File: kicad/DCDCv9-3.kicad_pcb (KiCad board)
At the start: 4 copper layers, 85.6 x 54 mm, 215 parts, among them J1 Screw_Terminal_01x03, J2 Conn_01x02_Male, J3 Conn_01x02, J4 Conn_01x02_Male, J5 XT60 Male, J6 Conn_01x02_Male, J7 Conn_01x02_Male, J8 Conn_01x02_Male, Q1 PMV20ENR, Q10 IMBG65R050M2HXTMA1, Q11 IMBG65R050M2HXTMA1, Q2 PMV20ENR, Q3 SIHP24N80AE-GE3, Q4 IXYP8N90C3, Q5 PMV20ENR, Q6 PMV20ENR, Q7 PMV20ENR, Q8 BSC027N06LS5ATMA1, Q9 BSC027N06LS5ATMA1, T1 DIY Transformer ETD 39, U1 TBA 1-1212HI, U10 LM2904BIDDFR, U11 UCC21520DW, U12 UCC25600, U13 ZXRE330ASA-7, U14 LM2904BIDDFR, U2 RT9058-90GVL, U3 MP4541_SOP8-EP, U4 TLV61048DBVR, U5 NCP4305DMTTWG, U6 LM2904BIDDFR, U7 TL431, U8 NCP4305DMTTWG, U9 ACPL-217-50AE

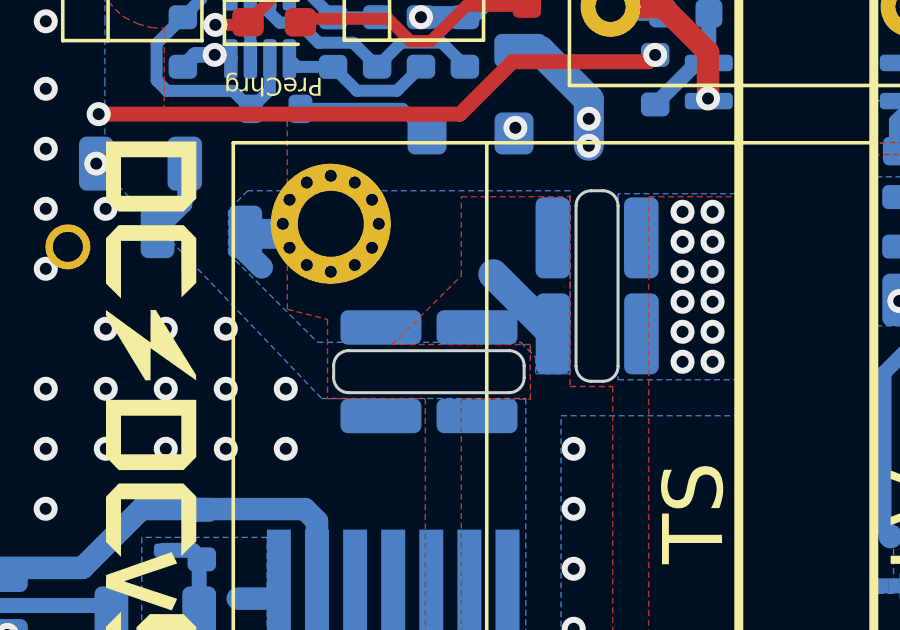
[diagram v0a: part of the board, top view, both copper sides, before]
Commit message: adjusted creepage distance
The closest inner layer to outer layer, which uses a prepreg of 0.21 mm, would result in 0.81 mm creepage distance on edges. Due to unknown IPC 2221 rating for this case, the design was adjusted (below the gate driver and a trace below the resonant capacitors) from 0.3 mm to 0.6 mm to be safe.
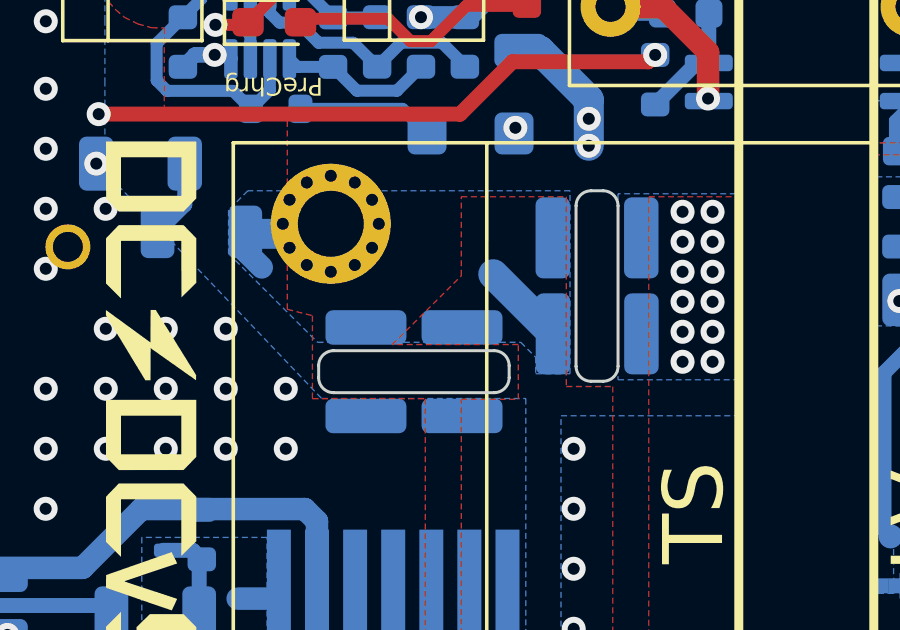
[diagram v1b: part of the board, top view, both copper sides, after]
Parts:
- moved C36 0.50 mm to (136.4, 96.4)
- moved C37 0.50 mm to (133.2, 96.4)
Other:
- outline, holes or cut-outs redrawn
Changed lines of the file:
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@@
 	(footprint "DCDC-Footprints:C_1210_3225Metric"
 		(layer "B.Cu")
-		(at 136.865 96.435 -90)
+		(at 136.365 96.435 -90)
 		(descr "Capacitor SMD 1210 (3225 Metric), square (rectangular) end terminal, IPC_7351 nominal, (Body size source: IPC-SM-782 page 76, https://www.pcb-3d.com/wordpress/wp-content/uploads/ipc-sm-782a_amendment_1_and_2.pdf), generated with kicad-footprint-generator")
 		(tags "capacitor")
@@
 	(footprint "DCDC-Footprints:C_1210_3225Metric"
 		(layer "B.Cu")
-		(at 133.661905 96.43674 -90)
+		(at 133.161905 96.43674 -90)
 		(descr "Capacitor SMD 1210 (3225 Metric), square (rectangular) end terminal, IPC_7351 nominal, (Body size source: IPC-SM-782 page 76, https://www.pcb-3d.com/wordpress/wp-content/uploads/ipc-sm-782a_amendment_1_and_2.pdf), generated with kicad-footprint-generator")
 		(tags "capacitor")
@@
 	)
 	(gr_line
-		(start 132.585 95.735)
-		(end 137.935 95.735)
+		(start 132.085 95.735)
+		(end 137.435 95.735)
 		(stroke
 			(width 0.1)
@@
 	)
 	(gr_arc
-		(start 132.585 97.135)
-		(mid 132.231447 96.988553)
-		(end 132.085 96.635)
+		(start 132.085 97.135)
+		(mid 131.731447 96.988553)
+		(end 131.585 96.635)
 		(stroke
 			(width 0.1)
@@
 	)
 	(gr_arc
-		(start 138.435 96.635)
-		(mid 138.288553 96.988553)
-		(end 137.935 97.135)
+		(start 137.935 96.635)
+		(mid 137.788553 96.988553)
+		(end 137.435 97.135)
 		(stroke
 			(width 0.1)
@@
 	)
 	(gr_arc
-		(start 137.935 95.735)
-		(mid 138.288553 95.881447)
-		(end 138.435 96.235)
+		(start 137.435 95.735)
+		(mid 137.788553 95.881447)
+		(end 137.935 96.235)
 		(stroke
 			(width 0.1)
@@
 	)
 	(gr_arc
-		(start 132.085 96.235)
-		(mid 132.231447 95.881447)
-		(end 132.585 95.735)
+		(start 131.585 96.235)
+		(mid 131.731447 95.881447)
+		(end 132.085 95.735)
 		(stroke
 			(width 0.1)
@@
 	)
 	(gr_line
-		(start 132.085 96.635)
-		(end 132.085 96.235)
+		(start 131.585 96.635)
+		(end 131.585 96.235)
 		(stroke
 			(width 0.1)
@@
 	)
 	(gr_line
-		(start 137.935 97.135)
-		(end 132.585 97.135)
+		(start 137.435 97.135)
+		(end 132.085 97.135)
 		(stroke
 			(width 0.1)
@@
 	)
 	(gr_line
-		(start 138.435 96.235)
-		(end 138.435 96.635)
+		(start 137.935 96.235)
+		(end 137.935 96.635)
 		(stroke
 			(width 0.1)
@@
 	)
 	(segment
-		(start 140.59 89.205)
-		(end 139.3 90.495)
+		(start 139.05 97.371855)
+		(end 137.396855 99.025)
 		(width 1)
 		(layer "In2.Cu")
@@
 	)
 	(segment
-		(start 137.396855 99.028145)
-		(end 137.396855 104.848145)
+		(start 140.59 88.905)
+		(end 140.59 88.955)
 		(width 1)
 		(layer "In2.Cu")
@@
 	(segment
 		(start 137.396855 104.848145)
-		(end 134.79 107.455)
+		(end 137.396855 99.025)
+		(width 1)
+		(layer "In2.Cu")
+		(net 56)
+	)
+	(segment
+		(start 140.59 88.955)
+		(end 139.05 90.495)
 		(width 1)
 		(layer "In2.Cu")
@@
 	)
 	(segment
-		(start 139.3 97.125)
-		(end 137.396855 99.028145)
+		(start 134.79 107.455)
+		(end 126.13 107.455)
 		(width 1)
 		(layer "In2.Cu")
@@
 	)
 	(segment
-		(start 140.59 89.205)
+		(start 140.59 88.905)
 		(end 140.59 88.005)
 		(width 1)
@@
 	)
 	(segment
-		(start 134.79 107.455)
-		(end 126.13 107.455)
+		(start 139.05 90.495)
+		(end 139.05 97.371855)
 		(width 1)
 		(layer "In2.Cu")
@@
 	)
 	(segment
-		(start 139.3 90.495)
-		(end 139.3 97.125)
+		(start 137.396855 104.848145)
+		(end 134.79 107.455)
 		(width 1)
 		(layer "In2.Cu")
@@
 		(hatch edge 0.508)
 		(connect_pads yes
-			(clearance 0.2)
+			(clearance 0.3)
 		)
 		(min_thickness 0.2)
@@
 				(xy 141.39 96.93) (xy 141.39 124.505) (xy 120.79 124.505) (xy 120.79 112.527097) (xy 117.84 112.527097)
 				(xy 117.84 109.055) (xy 127.73 109.055) (xy 127.73 107.105) (xy 136.34 107.105) (xy 136.34 97.355)
-				(xy 138.64 97.355) (xy 138.64 95.53) (xy 134.040127 95.53) (xy 136.34 93.241743) (xy 136.34 90.605)
-				(xy 139.965 90.605) (xy 139.965 96.93)
+				(xy 138.24 97.355) (xy 138.24 95.53) (xy 134.040127 95.53) (xy 136.34 93.241743) (xy 136.34 90.605)
+				(xy 139.84 90.605) (xy 139.84 96.93)
 			)
 		)
@@
 				(xy 124.237796 83.362886) (xy 124.26 83.455) (xy 124.345872 83.71) (xy 124.59 84.11) (xy 124.81986 84.37)
 				(xy 125.108608 84.62) (xy 125.561708 84.843826) (xy 126.021098 84.97) (xy 126.438931 84.98) (xy 126.438931 87.755)
-				(xy 130.54 87.755) (xy 130.54 94.355) (xy 130.537059 94.355) (xy 131.879563 94.695) (xy 131.880027 97.335)
+				(xy 130.54 87.755) (xy 130.54 94.355) (xy 130.537059 94.355) (xy 131.37864 94.568137) (xy 131.379126 97.335)
 				(xy 135.14 97.335) (xy 135.14 105.855) (xy 117.84 105.855) (xy 117.84 101.005) (xy 115.24 101.005)
 				(xy 115.24 101.33) (xy 106.89 101.33) (xy 106.89 95.705) (xy 107.14 95.705) (xy 107.14 83.755) (xy 108.39 82.505)
@@
 		(polygon
 			(pts
-				(xy 124.565 87.805) (xy 130.59 87.805) (xy 130.59 90.98) (xy 130.59 92.805) (xy 131.88 92.805) (xy 131.88 97.335)
+				(xy 124.565 87.805) (xy 130.59 87.805) (xy 130.59 90.98) (xy 130.59 92.805) (xy 131.38 92.805) (xy 131.38 97.335)
 				(xy 137.89 97.335) (xy 137.89 105.005) (xy 134.94 107.955) (xy 127.335531 107.955) (xy 127.335531 106.255)
-				(xy 117.89 106.255) (xy 117.89 101.005) (xy 115.24 101.005) (xy 115.24 108.205) (xy 102.79 108.205)
+				(xy 117.89 106.255) (xy 117.89 101.005) (xy 114.94 101.005) (xy 114.94 108.205) (xy 102.79 108.205)
 				(xy 102.79 101.505) (xy 100.29 101.505) (xy 100.29 95.705) (xy 107.14 95.705) (xy 107.14 83.755)
 				(xy 108.39 82.505) (xy 121.64 82.505) (xy 122.49 81.655) (xy 122.49 79.33) (xy 124.29909 79.33)
@@
 		(polygon
 			(pts
-				(xy 100.29 109.405) (xy 115.24 109.405) (xy 115.24 113.205) (xy 115.765 113.73) (xy 119.99 113.73)
+				(xy 100.29 109.405) (xy 114.94 109.405) (xy 114.94 112.905) (xy 115.765 113.73) (xy 119.99 113.73)
 				(xy 119.99 125.305) (xy 127.99 125.305) (xy 127.99 128.705) (xy 100.29 128.705)
 			)
@@
 		(polygon
 			(pts
-				(xy 124.565 87.805) (xy 130.59 87.805) (xy 130.59 92.805) (xy 131.88 92.805) (xy 131.88 97.335)
+				(xy 124.565 87.805) (xy 130.59 87.805) (xy 130.59 92.805) (xy 131.38 92.805) (xy 131.38 97.335)
 				(xy 135.84 97.335) (xy 135.84 104.33) (xy 134.015 106.155) (xy 117.84 106.155) (xy 117.84 101.005)
 				(xy 115.24 101.005) (xy 115.24 112.655) (xy 106.69 112.655) (xy 106.69 108.605) (xy 102.79 108.605)

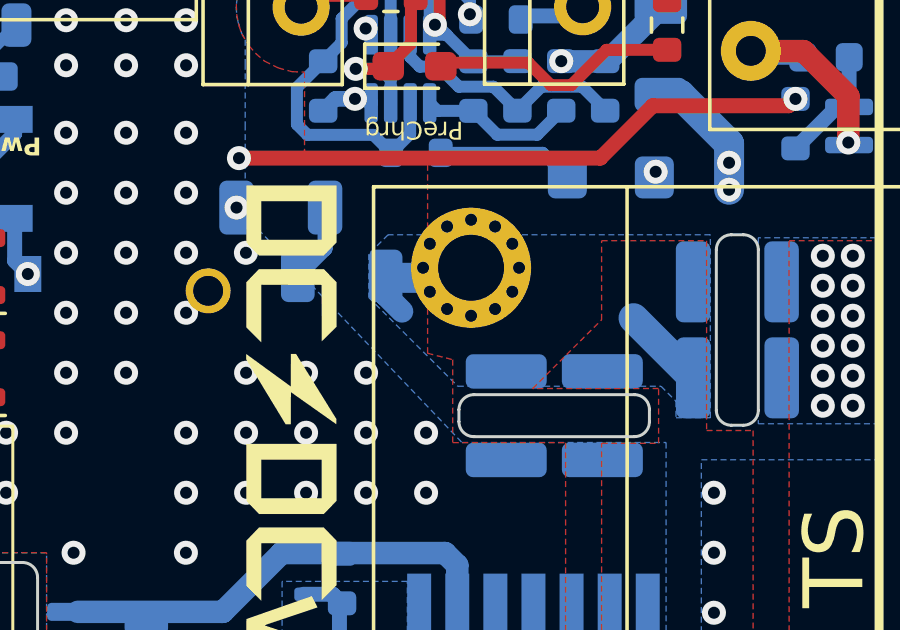
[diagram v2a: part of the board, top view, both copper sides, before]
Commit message: increased clearance a bit more
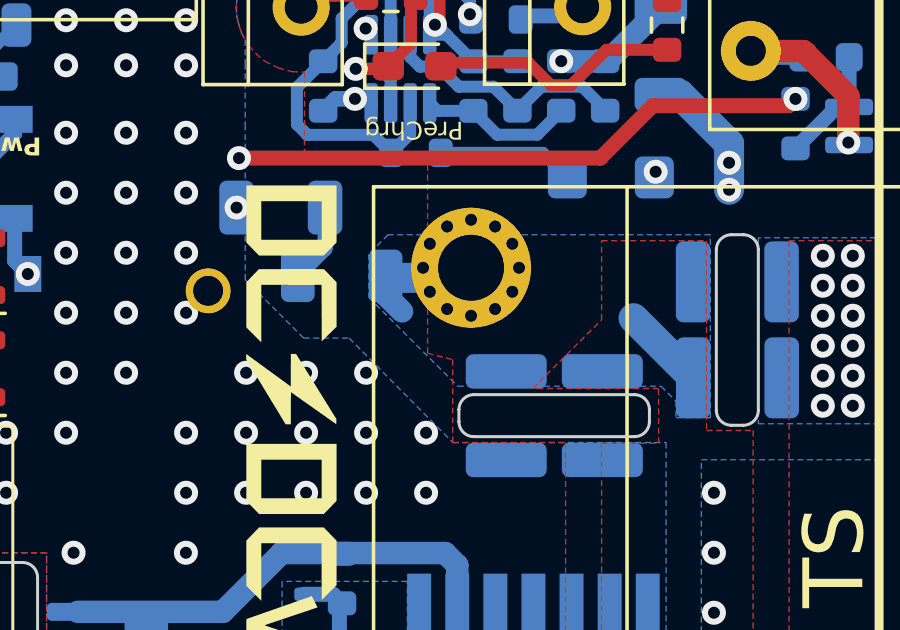
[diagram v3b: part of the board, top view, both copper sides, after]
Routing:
- net -HV_pc: vias 47 -> 46
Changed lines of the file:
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@@
 			(drillshape 0)
 			(scaleselection 1)
-			(outputdirectory "production/PDF Gerber Plot/")
+			(outputdirectory "production/PDF_Gerber_Plot/")
 		)
 	)
@@
 			(net 38 "Net-(C39-Pad2)")
 			(pintype "passive")
-			(clearance 0.6)
+			(clearance 1.2)
 		)
 		(model "${KICAD8_3DMODEL_DIR}/Capacitor_SMD.3dshapes/C_1206_3216Metric.wrl"
@@
 			(net 38 "Net-(C39-Pad2)")
 			(pintype "passive")
-			(clearance 0.6)
+			(clearance 1.2)
 		)
 		(pad "2" smd roundrect
@@
 	)
 	(via
-		(at 124.485 91.006167)
-		(size 0.8)
-		(drill 0.4)
-		(layers "F.Cu" "B.Cu")
-		(free yes)
-		(net 54)
-	)
-	(via
 		(at 120.49 95.005)
 		(size 0.8)
@@
 				(xy 124.670864 81.410864) (xy 124.409881 81.799881) (xy 124.26 82.18) (xy 124.19 82.505) (xy 124.16 82.805)
 				(xy 124.18 83.105) (xy 124.22 83.305) (xy 124.33 83.66) (xy 124.46 83.905) (xy 124.46 84.705) (xy 124.46 86.73)
-				(xy 124.46 88.83) (xy 124.46 89.769698) (xy 131.685957 97.33) (xy 138.49 97.33)
+				(xy 124.46 88.83) (xy 124.46 91.9) (xy 126.40967 93.849621) (xy 127.925 93.849483) (xy 131.38214 97.33)
+				(xy 138.49 97.33)
 			)
 		)

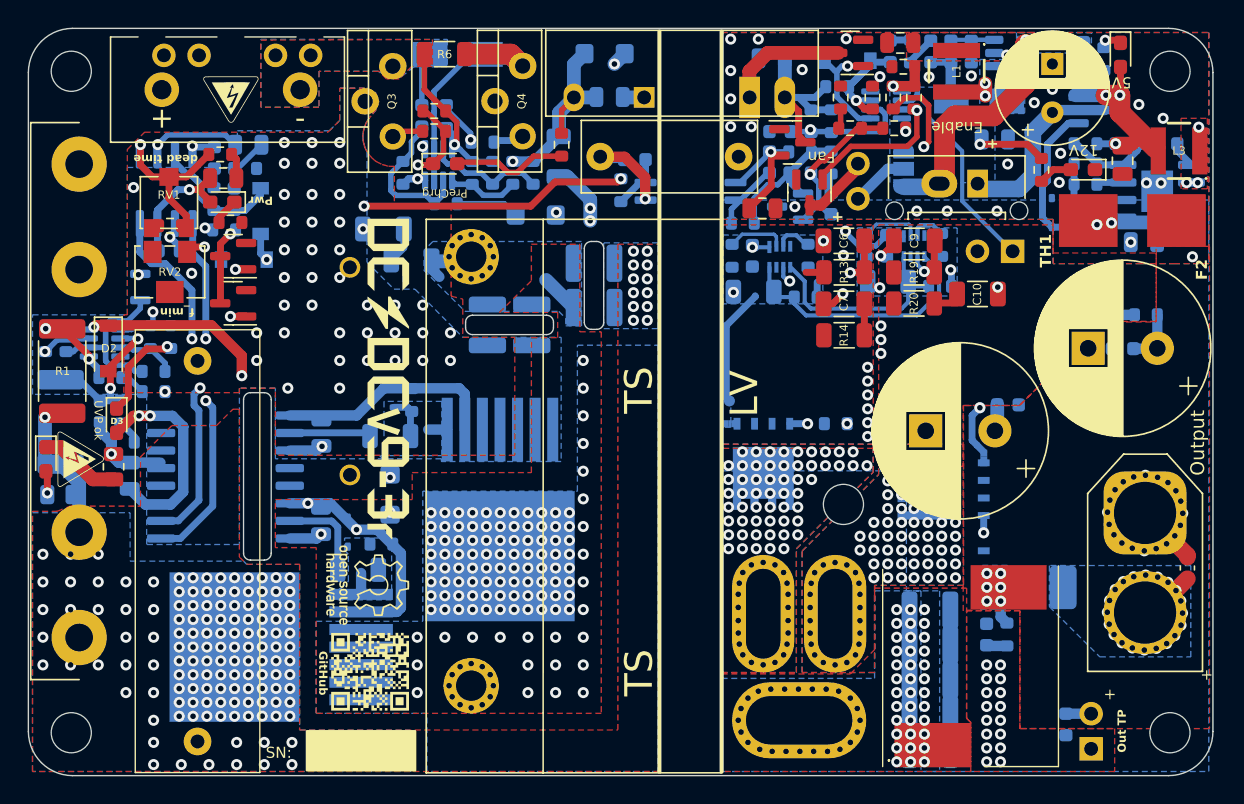
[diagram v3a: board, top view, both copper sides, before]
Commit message: Changed Mounting Holes from 2.9 mm to 3.0 mm
Changed Mounting Holes from 2.9 mm to 3.0 mm. Although 2.9 mm was a nice fit for M3 screws, increasing it a bit will help against manufacturing tolerances.
Note: The footprint originated from a M2.5 Footprint. Despite changing the diameter, the old name remained until now.
Rules note: T 10.1.2 does not apply (Minimum M4), als the DCDC is not part of any primary structure. However, if somebody really needs M4, it is totally possible to increase the hole size by drilling - there is enough distance between the hole and traces. Just make sure that any screw heads are not shorting anything. The use of M4 pan head screws might therefore not be possible.
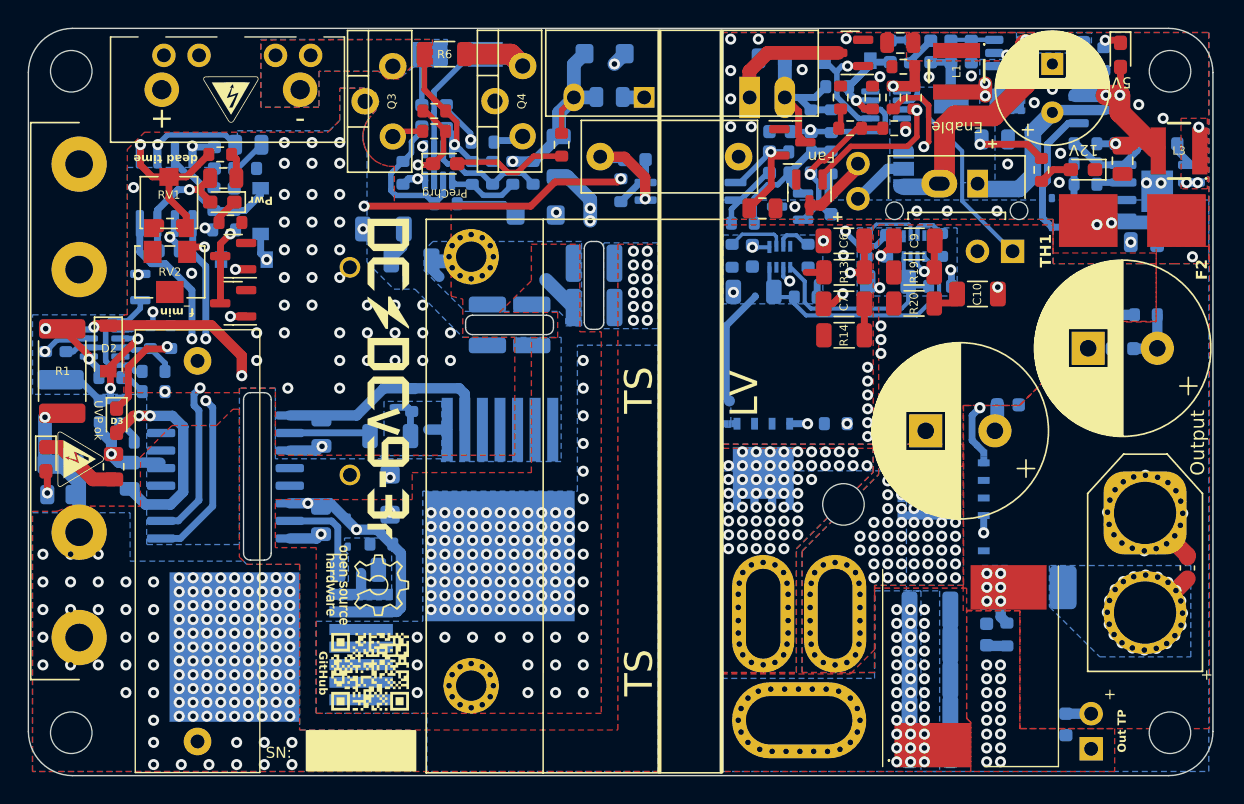
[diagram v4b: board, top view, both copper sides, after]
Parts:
- REF** (x5): value MountingHole_2.5mm -> MountingHole_M3_tight; footprint DCDC-Footprints:MountingHole_2.5mm -> DCDC-Footprints:MountingHole_M3_tight
